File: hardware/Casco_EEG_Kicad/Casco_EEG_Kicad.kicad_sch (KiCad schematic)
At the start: 0 parts

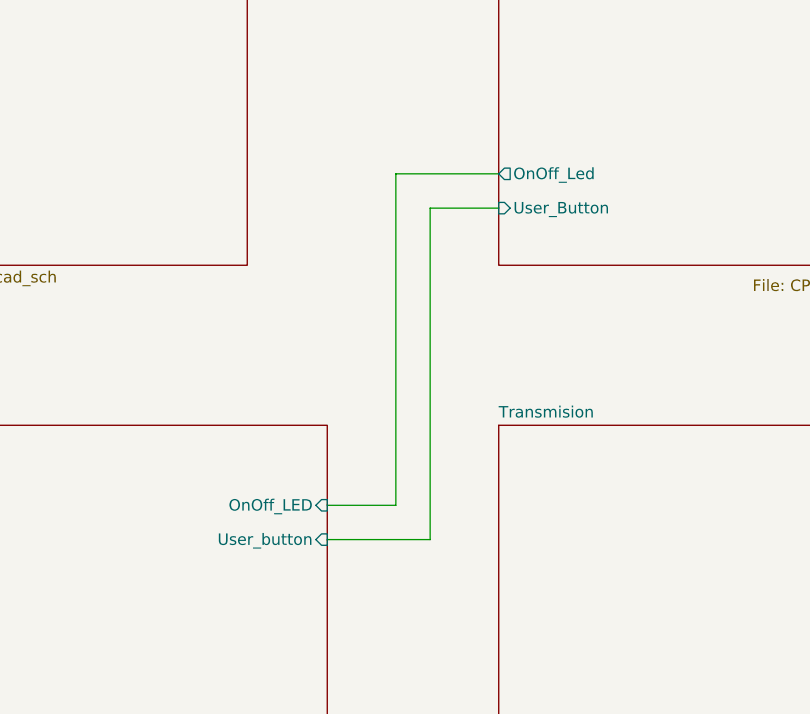
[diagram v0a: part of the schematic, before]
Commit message: Primera implementacion de PCB, cambios varios
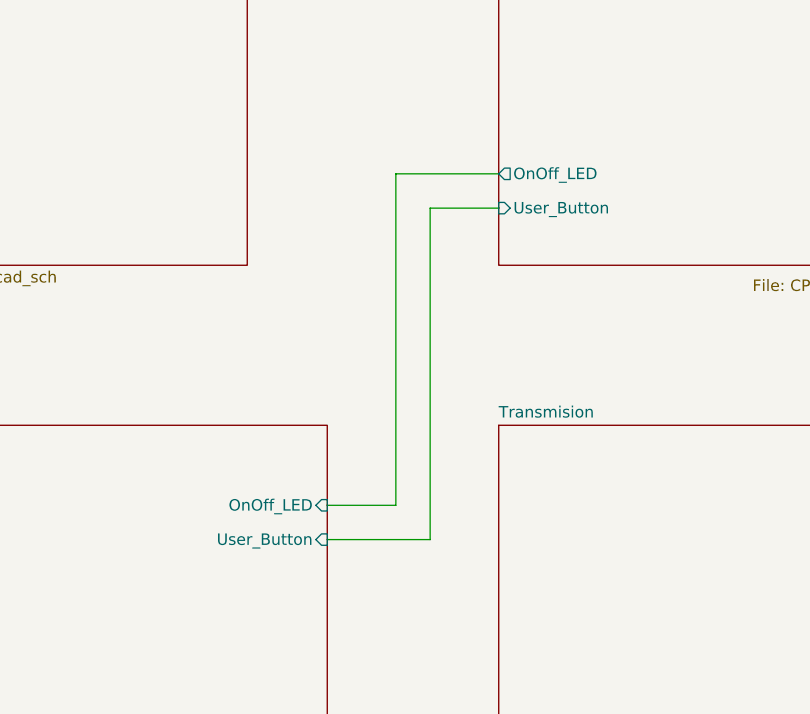
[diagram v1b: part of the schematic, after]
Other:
- sheet CPU ports: added OnOff_LED; removed OnOff_Led
- sheet Interfaz_Usuario ports: added User_Button; removed User_button
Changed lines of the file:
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@@
 			)
 		)
-		(pin "OnOff_Led" output
-			(at 109.22 87.63 180)
+		(pin "User_Button" input
+			(at 109.22 91.44 180)
 			(effects
 				(font
@@
 			)
 		)
-		(pin "User_Button" input
-			(at 109.22 91.44 180)
+		(pin "OnOff_LED" output
+			(at 109.22 87.63 180)
 			(effects
 				(font
@@
 			)
 		)
-		(pin "User_button" input
+		(pin "User_Button" input
 			(at 90.17 128.27 0)
 			(effects
